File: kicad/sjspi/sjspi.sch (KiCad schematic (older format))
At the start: 14 parts, among them J1 Conn_02x20_Odd_Even, J2 DB9_Female, U1 74LVC245

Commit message: v0.2 - fix pi connector position. Fix DB9 size. Connect level shifter's ground leg
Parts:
- J2: footprint Connector_Dsub:DSUB-9_Female_Horizontal_P2.77x2.84mm_EdgePinOffset9.40mm -> Connector_Dsub:DSUB-9_Female_Horizontal_P2.77x2.84mm_EdgePinOffset7.70mm_Housed_MountingHolesOffset9.12mm
- R1, R2, R3, R4, R5, R6: footprint Resistor_THT:R_Axial_DIN0204_L3.6mm_D1.6mm_P7.62mm_Horizontal -> Resistor_THT:R_Axial_DIN0309_L9.0mm_D3.2mm_P12.70mm_Horizontal
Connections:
- net GND: now also U1.19 (~OE)
- net at U1.2 (A1): now also J1.37 (Pin_37); no longer J1.8 (Pin_8)
- net at U1.3 (A2): now also J1.31 (Pin_31); no longer J1.10 (Pin_10)
- net at U1.4 (A3): now also J1.29 (Pin_29); no longer J1.12 (Pin_12)
- net at U1.5 (A4): now also J1.15 (Pin_15); no longer J1.16 (Pin_16)
- net at U1.6 (A5): now also J1.13 (Pin_13); no longer J1.18 (Pin_18)
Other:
- moved on the sheet: J1

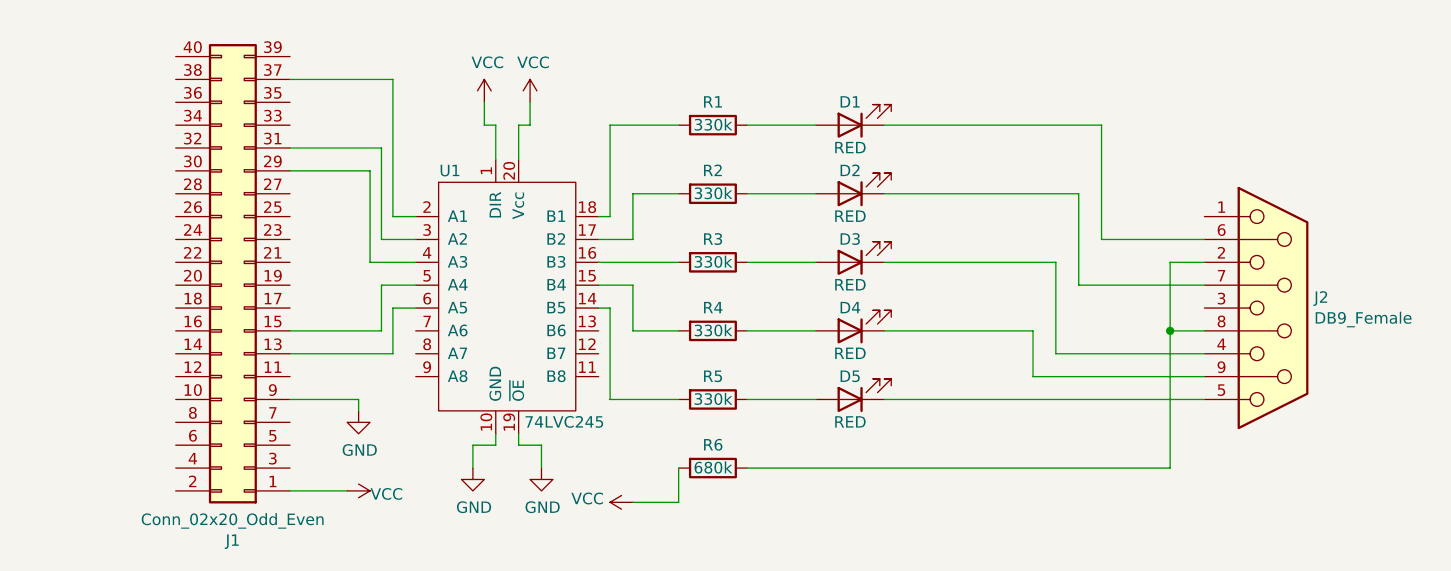
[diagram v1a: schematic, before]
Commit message: v0.3 - fix resistors values
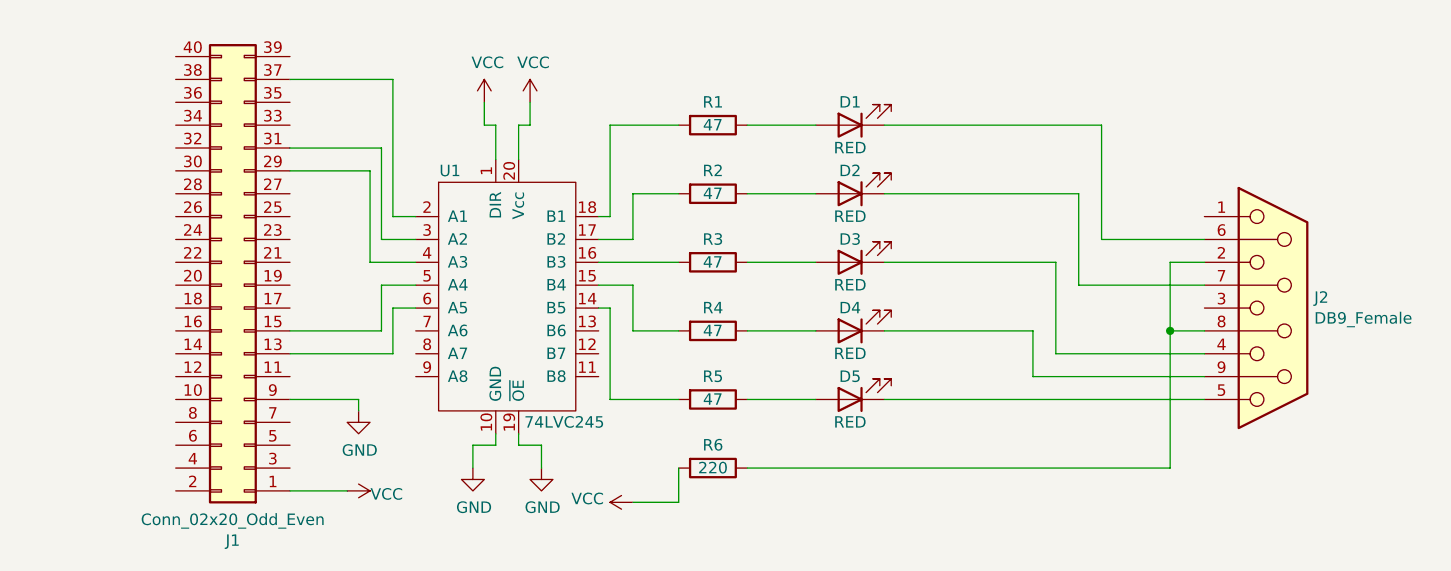
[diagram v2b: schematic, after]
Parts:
- R1, R2, R3, R4, R5: value 330k -> 47
- R6: value 680k -> 220
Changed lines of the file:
@@
 Sheet 1 1
 Title "SJSPi"
-Date "2021-06-13"
-Rev "v0.2"
+Date "2021-06-27"
+Rev "v0.3"
 Comp ""
 Comment1 ""
@@
 P 6900 3100
 F 0 "R1" V 6800 3100 50  0000 C CNN
-F 1 "330k" V 6900 3100 50  0000 C CNN
+F 1 "47" V 6900 3100 50  0000 C CNN
 F 2 "Resistor_THT:R_Axial_DIN0309_L9.0mm_D3.2mm_P12.70mm_Horizontal" V 6830 3100 50  0001 C CNN
 F 3 "~" H 6900 3100 50  0001 C CNN
@@
 P 6900 3400
 F 0 "R2" V 6800 3400 50  0000 C CNN
-F 1 "330k" V 6900 3400 50  0000 C CNN
+F 1 "47" V 6900 3400 50  0000 C CNN
 F 2 "Resistor_THT:R_Axial_DIN0309_L9.0mm_D3.2mm_P12.70mm_Horizontal" V 6830 3400 50  0001 C CNN
 F 3 "~" H 6900 3400 50  0001 C CNN
@@
 P 6900 3700
 F 0 "R3" V 6800 3700 50  0000 C CNN
-F 1 "330k" V 6900 3700 50  0000 C CNN
+F 1 "47" V 6900 3700 50  0000 C CNN
 F 2 "Resistor_THT:R_Axial_DIN0309_L9.0mm_D3.2mm_P12.70mm_Horizontal" V 6830 3700 50  0001 C CNN
 F 3 "~" H 6900 3700 50  0001 C CNN
@@
 P 6900 4000
 F 0 "R4" V 6800 4000 50  0000 C CNN
-F 1 "330k" V 6900 4000 50  0000 C CNN
+F 1 "47" V 6900 4000 50  0000 C CNN
 F 2 "Resistor_THT:R_Axial_DIN0309_L9.0mm_D3.2mm_P12.70mm_Horizontal" V 6830 4000 50  0001 C CNN
 F 3 "~" H 6900 4000 50  0001 C CNN
@@
 P 6900 4300
 F 0 "R5" V 6800 4300 50  0000 C CNN
-F 1 "330k" V 6900 4300 50  0000 C CNN
+F 1 "47" V 6900 4300 50  0000 C CNN
 F 2 "Resistor_THT:R_Axial_DIN0309_L9.0mm_D3.2mm_P12.70mm_Horizontal" V 6830 4300 50  0001 C CNN
 F 3 "~" H 6900 4300 50  0001 C CNN
@@
 P 6900 4600
 F 0 "R6" V 6800 4600 50  0000 C CNN
-F 1 "680k" V 6900 4600 50  0000 C CNN
+F 1 "220" V 6900 4600 50  0000 C CNN
 F 2 "Resistor_THT:R_Axial_DIN0309_L9.0mm_D3.2mm_P12.70mm_Horizontal" V 6830 4600 50  0001 C CNN
 F 3 "~" H 6900 4600 50  0001 C CNN

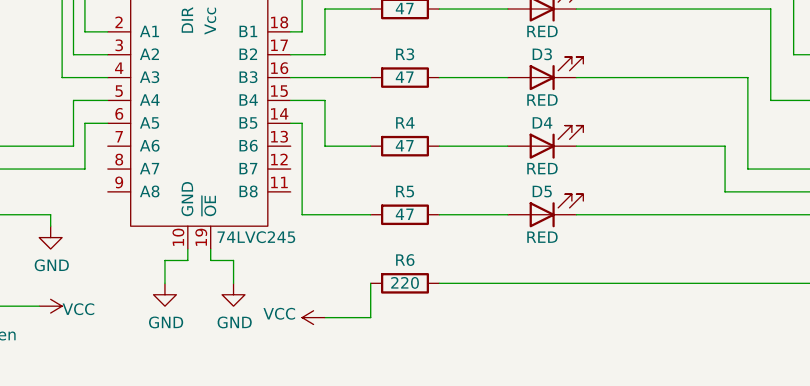
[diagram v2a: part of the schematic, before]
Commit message: v0.3 - fix resistors values
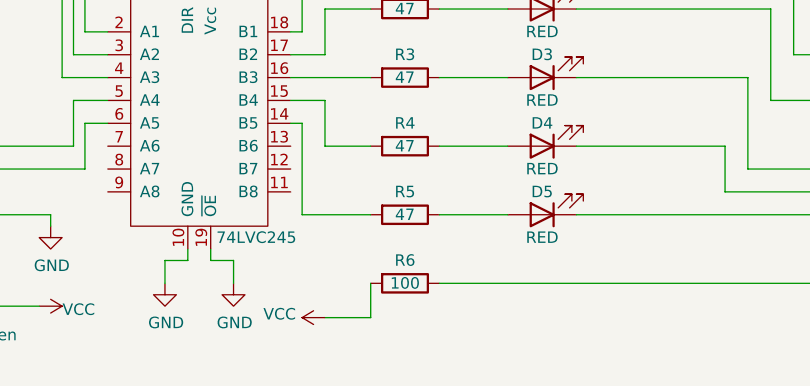
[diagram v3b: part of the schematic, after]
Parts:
- R6: value 220 -> 100
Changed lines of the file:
@@
 P 6900 4600
 F 0 "R6" V 6800 4600 50  0000 C CNN
-F 1 "220" V 6900 4600 50  0000 C CNN
+F 1 "100" V 6900 4600 50  0000 C CNN
 F 2 "Resistor_THT:R_Axial_DIN0309_L9.0mm_D3.2mm_P12.70mm_Horizontal" V 6830 4600 50  0001 C CNN
 F 3 "~" H 6900 4600 50  0001 C CNN
